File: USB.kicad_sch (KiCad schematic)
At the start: 8 parts, among them J11 USB_B_Micro, U9 CP2102N-A01-GQFN24

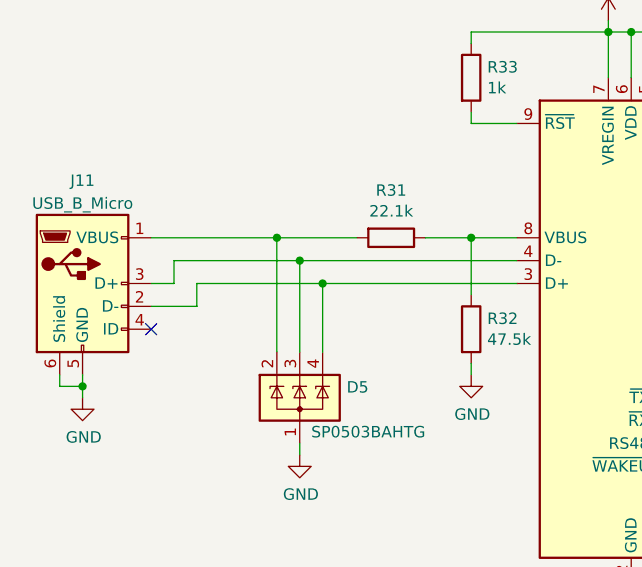
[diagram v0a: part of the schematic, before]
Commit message: merged v2.1 changes
removes external RTC, cleaned up big errors, only minor warnings remain
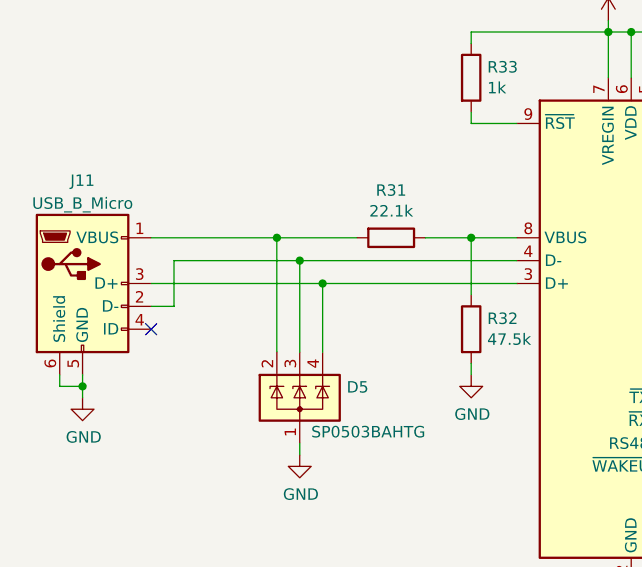
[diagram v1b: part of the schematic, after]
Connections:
- net at D5.4 (K), U9.3 (D+): now also J11.3 (D+); no longer J11.2 (D-)
- net at D5.3 (K), U9.4 (D-): now also J11.2 (D-); no longer J11.3 (D+)
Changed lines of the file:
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@@
-    (stroke (width 0) (type default))
-  )
-  (wire (pts (xy 99.06 98.425) (xy 96.52 98.425))
     (stroke (width 0) (type default))
   )
@@
     (stroke (width 0) (type default))
   )
+  (wire (pts (xy 96.52 98.425) (xy 115.57 98.425))
+    (stroke (width 0) (type default))
+  )
   (wire (pts (xy 113.03 117.475) (xy 113.03 116.205))
     (stroke (width 0) (type default))
@@
     (stroke (width 0) (type default))
   )
-  (wire (pts (xy 96.52 100.965) (xy 101.6 100.965))
+  (wire (pts (xy 96.52 100.965) (xy 99.06 100.965))
     (stroke (width 0) (type default))
   )
@@
     (stroke (width 0) (type default))
   )
-  (wire (pts (xy 101.6 98.425) (xy 115.57 98.425))
-    (stroke (width 0) (type default))
-  )
   (wire (pts (xy 200.025 70.485) (xy 187.325 70.485))
     (stroke (width 0) (type default))
   )
-  (wire (pts (xy 101.6 100.965) (xy 101.6 98.425))
+  (wire (pts (xy 99.06 95.885) (xy 99.06 100.965))
     (stroke (width 0) (type default))
   )
@@
     (stroke (width 0) (type default))
   )
-  (wire (pts (xy 99.06 95.885) (xy 99.06 98.425))
-    (stroke (width 0) (type default))
-  )

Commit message: cleaner, still needs full checklisting
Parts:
- J11: footprint Connector_USB:USB_Micro-B_Molex-105017-0001 -> UTSVT_Connectors:USB_Micro-B_Molex-105017-0001
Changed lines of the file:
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@@
       (effects (font (size 1.27 1.27)))
     )
-    (property "Footprint" "Connector_USB:USB_Micro-B_Molex-105017-0001" (at 92.71 99.695 0)
+    (property "Footprint" "UTSVT_Connectors:USB_Micro-B_Molex-105017-0001" (at 92.71 99.695 0)
       (effects (font (size 1.27 1.27)) hide)
     )

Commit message: bom, gerbers, edge cuts, footprint verification
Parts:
- C40: P/N (none) -> 08055D475KAT2A
- C41: P/N (none) -> C0805C104K5RAC7411
- D5: P/N (none) -> SP0503BAHTG
- R31: P/N (none) -> CRCW080522K1FKEA
- R32: P/N (none) -> CRCW080547K5FKEA
- R33: P/N (none) -> CRCW08051K00FKEA
- U9: value CP2102N-A01-GQFN24 -> CP2102N-A02-GQFN24; P/N (none) -> CP2102N-A02-GQFN24
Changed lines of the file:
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@@
       (effects (font (size 1.27 1.27)))
     )
-    (property "Value" "CP2102N-A01-GQFN24" (at 149.86 61.595 0)
+    (property "Value" "CP2102N-A02-GQFN24" (at 149.86 61.595 0)
       (effects (font (size 1.27 1.27)))
     )
@@
       (effects (font (size 1.27 1.27)) (justify left) hide)
     )
-    (property "Datasheet" "http://www.silabs.com/support%20documents/technicaldocs/cp2102n-datasheet.pdf" (at 151.13 130.175 0)
+    (property "Datasheet" "https://www.mouser.com/datasheet/2/368/cp2102n_datasheet-1634912.pdf" (at 151.13 130.175 0)
+      (effects (font (size 1.27 1.27)) hide)
+    )
+    (property "P/N" "CP2102N-A02-GQFN24" (at 149.86 103.505 0)
       (effects (font (size 1.27 1.27)) hide)
     )
@@
       (effects (font (size 1.27 1.27)) hide)
     )
-    (property "Datasheet" "~" (at 92.71 99.695 0)
+    (property "Datasheet" "https://www.mouser.com/datasheet/2/276/1/1050170001_IO_CONNECTORS-230168.pdf" (at 92.71 99.695 0)
       (effects (font (size 1.27 1.27)) hide)
     )
@@
       (effects (font (size 1.27 1.27)) (justify left) hide)
     )
-    (property "Datasheet" "http://www.littelfuse.com/~/media/files/littelfuse/technical%20resources/documents/data%20sheets/sp05xxba.pdf" (at 116.205 107.95 0)
+    (property "Datasheet" "https://www.mouser.com/datasheet/2/240/Littelfuse_TVS_Diode_Array_SP05_Datasheet_pdf-777043.pdf" (at 116.205 107.95 0)
+      (effects (font (size 1.27 1.27)) hide)
+    )
+    (property "P/N" "SP0503BAHTG" (at 113.03 111.125 0)
       (effects (font (size 1.27 1.27)) hide)
     )
@@
       (effects (font (size 1.27 1.27)) hide)
     )
-    (property "Datasheet" "~" (at 132.08 103.505 0)
+    (property "Datasheet" "https://www.mouser.com/datasheet/2/427/dcrcwe3-1762152.pdf" (at 132.08 103.505 0)
+      (effects (font (size 1.27 1.27)) hide)
+    )
+    (property "P/N" "CRCW080547K5FKEA" (at 132.08 103.505 0)
       (effects (font (size 1.27 1.27)) hide)
     )
@@
       (effects (font (size 1.27 1.27)) hide)
     )
-    (property "Datasheet" "~" (at 123.19 93.345 0)
+    (property "Datasheet" "https://www.mouser.com/datasheet/2/427/dcrcwe3-1762152.pdf" (at 123.19 93.345 0)
+      (effects (font (size 1.27 1.27)) hide)
+    )
+    (property "P/N" "CRCW080522K1FKEA" (at 123.19 93.345 0)
       (effects (font (size 1.27 1.27)) hide)
     )
@@
       (effects (font (size 1.27 1.27)) hide)
     )
-    (property "Datasheet" "~" (at 132.08 75.565 0)
+    (property "Datasheet" "https://www.mouser.com/datasheet/2/427/dcrcwe3-1762152.pdf" (at 132.08 75.565 0)
+      (effects (font (size 1.27 1.27)) hide)
+    )
+    (property "P/N" "CRCW08051K00FKEA" (at 132.08 75.565 0)
       (effects (font (size 1.27 1.27)) hide)
     )
@@
       (effects (font (size 1.27 1.27)) hide)
     )
-    (property "Datasheet" "~" (at 187.325 75.565 0)
+    (property "Datasheet" "https://www.mouser.com/datasheet/2/40/cx5r-2835979.pdf" (at 187.325 75.565 0)
+      (effects (font (size 1.27 1.27)) hide)
+    )
+    (property "P/N" "08055D475KAT2A" (at 187.325 75.565 0)
       (effects (font (size 1.27 1.27)) hide)
     )
@@
       (effects (font (size 1.27 1.27)) hide)
     )
-    (property "Datasheet" "~" (at 200.025 75.565 0)
-      (effects (font (size 1.27 1.27)) hide)
-    )
+    (property "Datasheet" "https://www.mouser.com/datasheet/2/212/KEM_C1002_X7R_SMD-1102033.pdf" (at 200.025 75.565 0)
+      (effects (font (size 1.27 1.27)) hide)
+    )
+    (property "P/N" "C0805C104K5RAC7411" (at 200.025 75.565 0)
+      (effects (font (size 1.27 1.27)) hide)
+    )

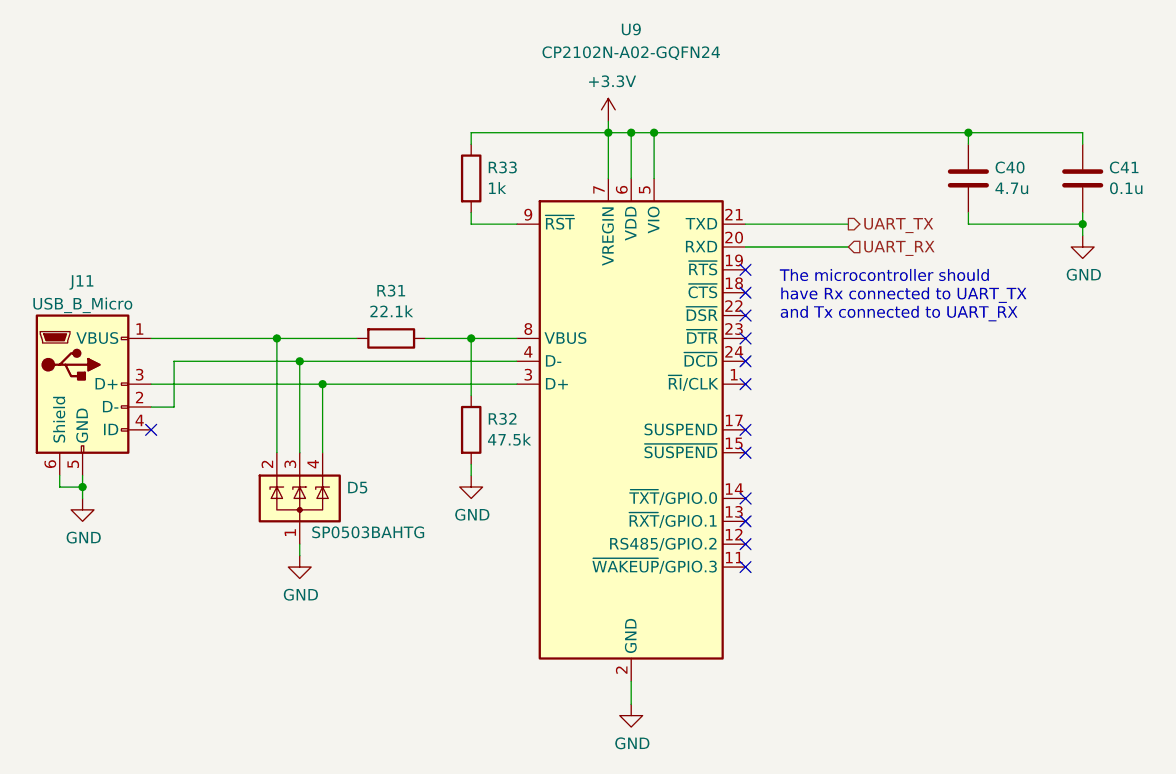
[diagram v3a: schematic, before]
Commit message: bluetooth schematic additions
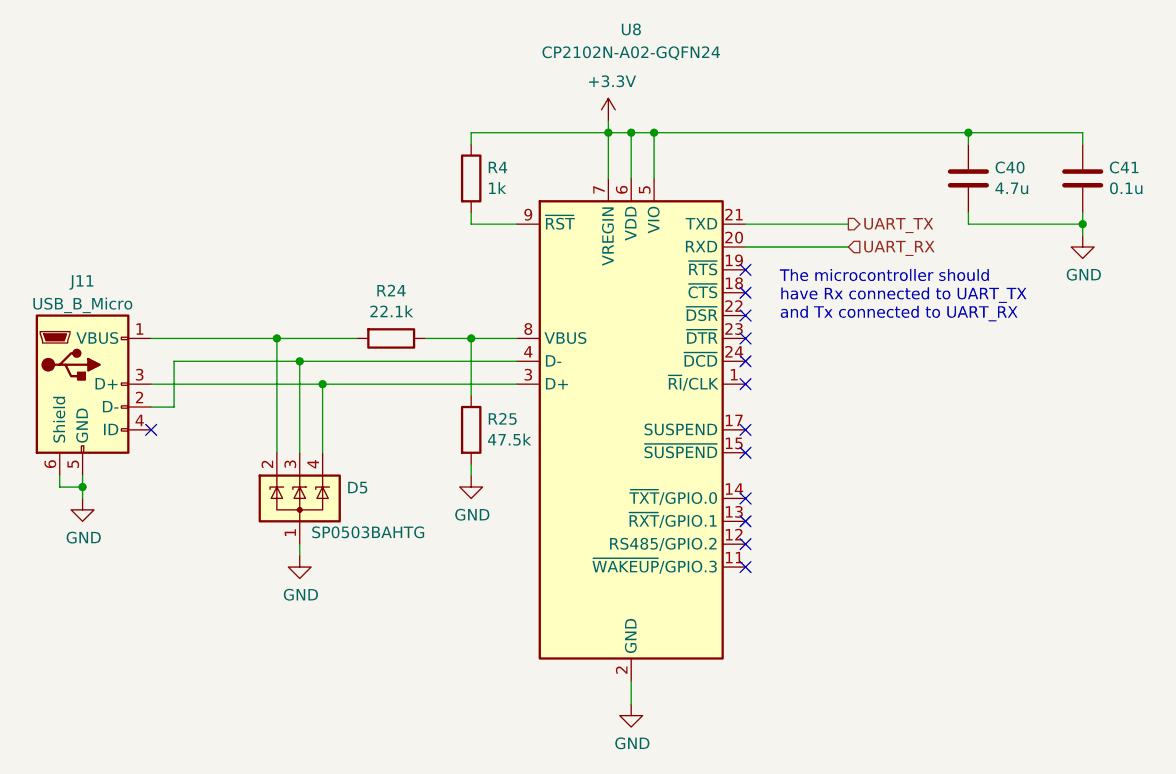
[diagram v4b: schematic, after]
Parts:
- renumbered R31 to R24, R32 to R25, R33 to R4, U9 to U8
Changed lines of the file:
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@@
   (symbol (lib_id "Interface_USB:CP2102N-Axx-xQFN24") (at 149.86 103.505 0) (unit 1)
     (in_bom yes) (on_board yes) (dnp no)
-    (property "Reference" "U9" (at 149.86 59.055 0)
+    (property "Reference" "U8" (at 149.86 59.055 0)
       (effects (font (size 1.27 1.27)))
     )
@@
     (instances
       (project "Telemetry-Primary"
-        (path "/7f2a449b-14af-42b3-8d38-5f0f8a5ee7ce/00000000-0000-0000-0000-00005f6d5b75"
-          (reference "U9") (unit 1)
+        (path "/7f2a449b-14af-42b3-8d38-5f0f8a5ee7ce/65ccd205-e43e-414f-91f4-e0a7c33b5687"
+          (reference "U8") (unit 1)
         )
       )
@@
     (instances
       (project "Telemetry-Primary"
-        (path "/7f2a449b-14af-42b3-8d38-5f0f8a5ee7ce/00000000-0000-0000-0000-00005f6d5b75"
-          (reference "J11") (unit 1)
-        )
         (path "/7f2a449b-14af-42b3-8d38-5f0f8a5ee7ce"
           (reference "J11") (unit 1)
         )
+        (path "/7f2a449b-14af-42b3-8d38-5f0f8a5ee7ce/65ccd205-e43e-414f-91f4-e0a7c33b5687"
+          (reference "J6") (unit 1)
+        )
       )
     )
@@
   (symbol (lib_id "power:GND") (at 88.9 111.125 0) (unit 1)
     (in_bom yes) (on_board yes) (dnp no)
-    (property "Reference" "#PWR0166" (at 88.9 117.475 0)
+    (property "Reference" "#PWR021" (at 88.9 117.475 0)
       (effects (font (size 1.27 1.27)) hide)
     )
@@
     (instances
       (project "Telemetry-Primary"
-        (path "/7f2a449b-14af-42b3-8d38-5f0f8a5ee7ce/00000000-0000-0000-0000-00005f6d5b75"
-          (reference "#PWR0166") (unit 1)
+        (path "/7f2a449b-14af-42b3-8d38-5f0f8a5ee7ce/65ccd205-e43e-414f-91f4-e0a7c33b5687"
+          (reference "#PWR021") (unit 1)
         )
       )
@@
   (symbol (lib_id "power:GND") (at 149.86 133.985 0) (unit 1)
     (in_bom yes) (on_board yes) (dnp no)
-    (property "Reference" "#PWR0167" (at 149.86 140.335 0)
+    (property "Reference" "#PWR023" (at 149.86 140.335 0)
       (effects (font (size 1.27 1.27)) hide)
     )
@@
     (instances
       (project "Telemetry-Primary"
-        (path "/7f2a449b-14af-42b3-8d38-5f0f8a5ee7ce/00000000-0000-0000-0000-00005f6d5b75"
-          (reference "#PWR0167") (unit 1)
+        (path "/7f2a449b-14af-42b3-8d38-5f0f8a5ee7ce/65ccd205-e43e-414f-91f4-e0a7c33b5687"
+          (reference "#PWR023") (unit 1)
         )
       )
@@
     (instances
       (project "Telemetry-Primary"
-        (path "/7f2a449b-14af-42b3-8d38-5f0f8a5ee7ce/00000000-0000-0000-0000-00005f6d5b75"
+        (path "/7f2a449b-14af-42b3-8d38-5f0f8a5ee7ce/65ccd205-e43e-414f-91f4-e0a7c33b5687"
           (reference "D5") (unit 1)
         )
@@
   (symbol (lib_id "power:GND") (at 113.03 117.475 0) (unit 1)
     (in_bom yes) (on_board yes) (dnp no)
-    (property "Reference" "#PWR0168" (at 113.03 123.825 0)
+    (property "Reference" "#PWR022" (at 113.03 123.825 0)
       (effects (font (size 1.27 1.27)) hide)
     )
@@
     (instances
       (project "Telemetry-Primary"
-        (path "/7f2a449b-14af-42b3-8d38-5f0f8a5ee7ce/00000000-0000-0000-0000-00005f6d5b75"
-          (reference "#PWR0168") (unit 1)
+        (path "/7f2a449b-14af-42b3-8d38-5f0f8a5ee7ce/65ccd205-e43e-414f-91f4-e0a7c33b5687"
+          (reference "#PWR022") (unit 1)
         )
       )
@@
   (symbol (lib_id "Device:R") (at 132.08 103.505 0) (unit 1)
     (in_bom yes) (on_board yes) (dnp no)
-    (property "Reference" "R32" (at 133.858 102.3366 0)
+    (property "Reference" "R25" (at 133.858 102.3366 0)
       (effects (font (size 1.27 1.27)) (justify left))
     )
@@
     (instances
       (project "Telemetry-Primary"
-        (path "/7f2a449b-14af-42b3-8d38-5f0f8a5ee7ce/00000000-0000-0000-0000-00005f6d5b75"
-          (reference "R32") (unit 1)
+        (path "/7f2a449b-14af-42b3-8d38-5f0f8a5ee7ce/65ccd205-e43e-414f-91f4-e0a7c33b5687"
+          (reference "R25") (unit 1)
         )
       )
@@
   (symbol (lib_id "Device:R") (at 123.19 93.345 270) (unit 1)
     (in_bom yes) (on_board yes) (dnp no)
-    (property "Reference" "R31" (at 123.19 88.0872 90)
+    (property "Reference" "R24" (at 123.19 88.0872 90)
       (effects (font (size 1.27 1.27)))
     )
@@
     (instances
       (project "Telemetry-Primary"
-        (path "/7f2a449b-14af-42b3-8d38-5f0f8a5ee7ce/00000000-0000-0000-0000-00005f6d5b75"
-          (reference "R31") (unit 1)
+        (path "/7f2a449b-14af-42b3-8d38-5f0f8a5ee7ce/65ccd205-e43e-414f-91f4-e0a7c33b5687"
+          (reference "R24") (unit 1)
         )
       )
@@
   (symbol (lib_id "power:GND") (at 132.08 108.585 0) (unit 1)
     (in_bom yes) (on_board yes) (dnp no)
-    (property "Reference" "#PWR0169" (at 132.08 114.935 0)
+    (property "Reference" "#PWR020" (at 132.08 114.935 0)
       (effects (font (size 1.27 1.27)) hide)
     )
@@
     (instances
       (project "Telemetry-Primary"
-        (path "/7f2a449b-14af-42b3-8d38-5f0f8a5ee7ce/00000000-0000-0000-0000-00005f6d5b75"
-          (reference "#PWR0169") (unit 1)
+        (path "/7f2a449b-14af-42b3-8d38-5f0f8a5ee7ce/65ccd205-e43e-414f-91f4-e0a7c33b5687"
+          (reference "#PWR020") (unit 1)
         )
       )
@@
   (symbol (lib_id "power:+3.3V") (at 147.32 69.215 0) (unit 1)
     (in_bom yes) (on_board yes) (dnp no)
-    (property "Reference" "#PWR0170" (at 147.32 73.025 0)
+    (property "Reference" "#PWR018" (at 147.32 73.025 0)
       (effects (font (size 1.27 1.27)) hide)
     )
@@
     (instances
       (project "Telemetry-Primary"
-        (path "/7f2a449b-14af-42b3-8d38-5f0f8a5ee7ce/00000000-0000-0000-0000-00005f6d5b75"
-          (reference "#PWR0170") (unit 1)
+        (path "/7f2a449b-14af-42b3-8d38-5f0f8a5ee7ce/65ccd205-e43e-414f-91f4-e0a7c33b5687"
+          (reference "#PWR018") (unit 1)
         )
       )
@@
   (symbol (lib_id "Device:R") (at 132.08 75.565 0) (unit 1)
     (in_bom yes) (on_board yes) (dnp no)
-    (property "Reference" "R33" (at 133.858 74.3966 0)
+    (property "Reference" "R4" (at 133.858 74.3966 0)
       (effects (font (size 1.27 1.27)) (justify left))
     )
@@
     (instances
       (project "Telemetry-Primary"
-        (path "/7f2a449b-14af-42b3-8d38-5f0f8a5ee7ce/00000000-0000-0000-0000-00005f6d5b75"
-          (reference "R33") (unit 1)
+        (path "/7f2a449b-14af-42b3-8d38-5f0f8a5ee7ce/65ccd205-e43e-414f-91f4-e0a7c33b5687"
+          (reference "R4") (unit 1)
         )
       )
@@
     (instances
       (project "Telemetry-Primary"
-        (path "/7f2a449b-14af-42b3-8d38-5f0f8a5ee7ce/00000000-0000-0000-0000-00005f6d5b75"
+        (path "/7f2a449b-14af-42b3-8d38-5f0f8a5ee7ce/65ccd205-e43e-414f-91f4-e0a7c33b5687"
           (reference "C40") (unit 1)
         )
@@
     (instances
       (project "Telemetry-Primary"
-        (path "/7f2a449b-14af-42b3-8d38-5f0f8a5ee7ce/00000000-0000-0000-0000-00005f6d5b75"
+        (path "/7f2a449b-14af-42b3-8d38-5f0f8a5ee7ce/65ccd205-e43e-414f-91f4-e0a7c33b5687"
           (reference "C41") (unit 1)
         )
@@
   (symbol (lib_id "power:GND") (at 200.025 81.915 0) (unit 1)
     (in_bom yes) (on_board yes) (dnp no)
-    (property "Reference" "#PWR0172" (at 200.025 88.265 0)
+    (property "Reference" "#PWR019" (at 200.025 88.265 0)
       (effects (font (size 1.27 1.27)) hide)
     )
@@
     (instances
       (project "Telemetry-Primary"
-        (path "/7f2a449b-14af-42b3-8d38-5f0f8a5ee7ce/00000000-0000-0000-0000-00005f6d5b75"
-          (reference "#PWR0172") (unit 1)
-        )
-      )
+        (path "/7f2a449b-14af-42b3-8d38-5f0f8a5ee7ce/65ccd205-e43e-414f-91f4-e0a7c33b5687"
+          (reference "#PWR019") (unit 1)
+        )
+      )
